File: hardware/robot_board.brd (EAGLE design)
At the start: 95.2 x 72.1 mm, 132 parts, among them J1 POWER_JACKPTH, Q1 DMP2035U, Q2 DMP2035U, Q3 DMP2035U-7, Q4 DMP2035U-7, U1 FT232RL-BASICSSOP, U11 LM393, U12 LM393, U16 LM393, U17 ATMEGA325PA, U5 SIA907EDJT, U6 SIA907EDJT

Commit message: begin power layout
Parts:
- removed IC3: (no value), v-reg:78XXS
- removed U$2: SIA907EDJT, jseng:SC70T
- removed U$7: TLV70233, jseng:SOT-23-5
- added U2: SIA907EDJT, jseng:SC70T
- added U3: MIC5219, SparkFun-PowerIC:SOT23-5
- added U7: TLV70233, jseng:SOT-23-5
- C1, C2: value (none) -> 22pF
- R1, R10, R11, R12, R13, R14, R15, R16, R17, R18, R19, R2, R20, R21, R22, R3, R4, R47, R48, R49, R5, R50, R6, R7, R8, R9: value 220 -> 300
- R25, R30, R32, R33: value (none) -> 10K
- R43: value (none) -> 1K
- R44: value (none) -> 100K
- Y1: value (none) -> 16MHz
- moved POWER 82.5 mm to (92.7, 13.0), turned to 270 degrees
- moved D25 76.2 mm to (2.54, 57.1)
- moved R41 73.4 mm to (3.81, 62.5), turned to 0 degrees
- moved R40 70.6 mm to (19.8, 68.1)
- moved R43 42.0 mm to (88.1, 10.9), turned to 270 degrees
- moved R44 38.6 mm to (88.4, 18.8), turned to 270 degrees
- moved R34 37.1 mm to (87.6, 23.6), turned to 0 degrees
- moved Q2 34.0 mm to (83.1, 21.6), turned to 0 degrees
- moved R53 26.8 mm to (53.3, 43.2), turned to 90 degrees
- moved U1 24.9 mm to (47.2, 6.60)
- moved U5 20.1 mm to (71.6, 33.0), turned to 90 degrees
- moved U6 19.8 mm to (68.6, 35.8)
- moved R39 18.0 mm to (19.8, 65.3), turned to 180 degrees
- moved R33 17.9 mm to (72.4, 40.1), turned to 90 degrees
- moved F1 15.6 mm to (75.2, 18.3), turned to 0 degrees
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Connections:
- net GYRO_INT renamed ACCEL_INT
- removed net MAIN_PWR: C3.+, D25.A, JP6.1, JP6.2, JP6.3, JP6.4, R23.2, R25.2, U$7.P$1, U$7.P$3, U$9.2, U16.8, U5.P$3, U6.P$3
- removed net N$40: Q1.2, Q2.2, R44.1
- new net PWR_SW: Q1.2, Q2.2, R44.1, U2.P$3
- new net RX: U1.1, U17.28
- new net TX: U1.5, U17.27
- net 3V3: now also U7.P$4; no longer U$7.P$4
- net 5V: now also C3.+, D25.A, JP6.1, JP6.2, JP6.3, JP6.4, R23.2, R25.2, U$9.2, U5.P$3, U6.P$3, U7.P$1, U7.P$3
- net GND: now also U3.2, U7.P$2; no longer IC3.GND, U$7.P$2
- net HIGH_5V_REG: now also U3.5; no longer IC3.OUT
- net N$28: now also U2.P$1, U2.P$4; no longer U$2.P$1, U$2.P$4
- net USBGATE: now also U2.P$2, U2.P$5; no longer U$2.P$2, U$2.P$5
- net USB_5V: now also U16.8, U2.P$6; no longer U$2.P$6
- net VIN: now also R35.2
- net VIN_F: now also U3.1, U3.3; no longer IC3.IN, R35.2, U$2.P$3
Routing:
- net VIN_F: track 0.00 -> 26.0 mm
- net GND: track 2.54 -> 20.8 mm
- net N$9: track 0.00 -> 15.9 mm
- net VIN: track 0.00 -> 9.68 mm
- net N$33: track 0.00 -> 7.73 mm
- net N$43: track 0.00 -> 6.00 mm
- net N$51: track 0.00 -> 5.14 mm
- net PWR_SW: track 0.00 -> 4.48 mm
- net 5V: track 0.00 -> 3.89 mm
- net USB_5V: track 0.00 -> 2.56 mm
- net D5: track 2.54 -> 0.00 mm
- net HIGH_5V_REG: track 0.00 -> 1.48 mm

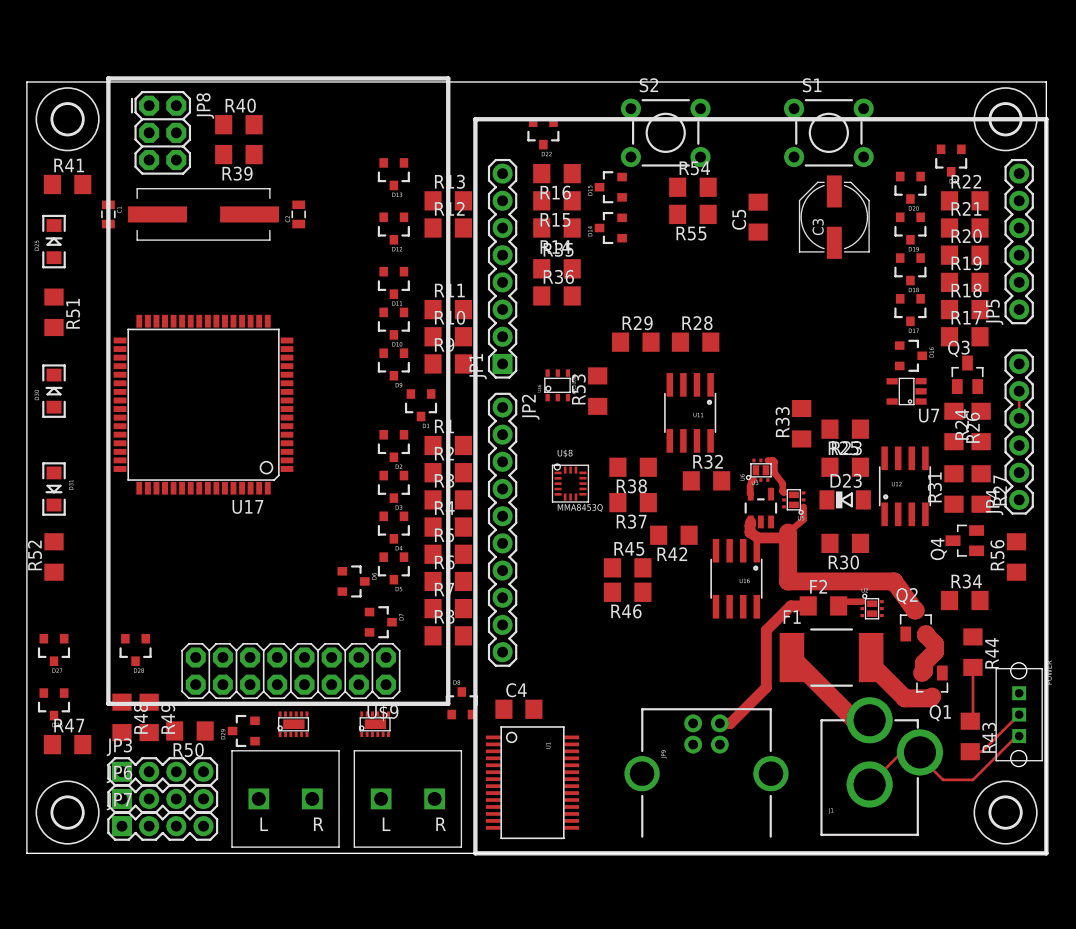
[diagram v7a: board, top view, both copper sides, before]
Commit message: more routing and library updates
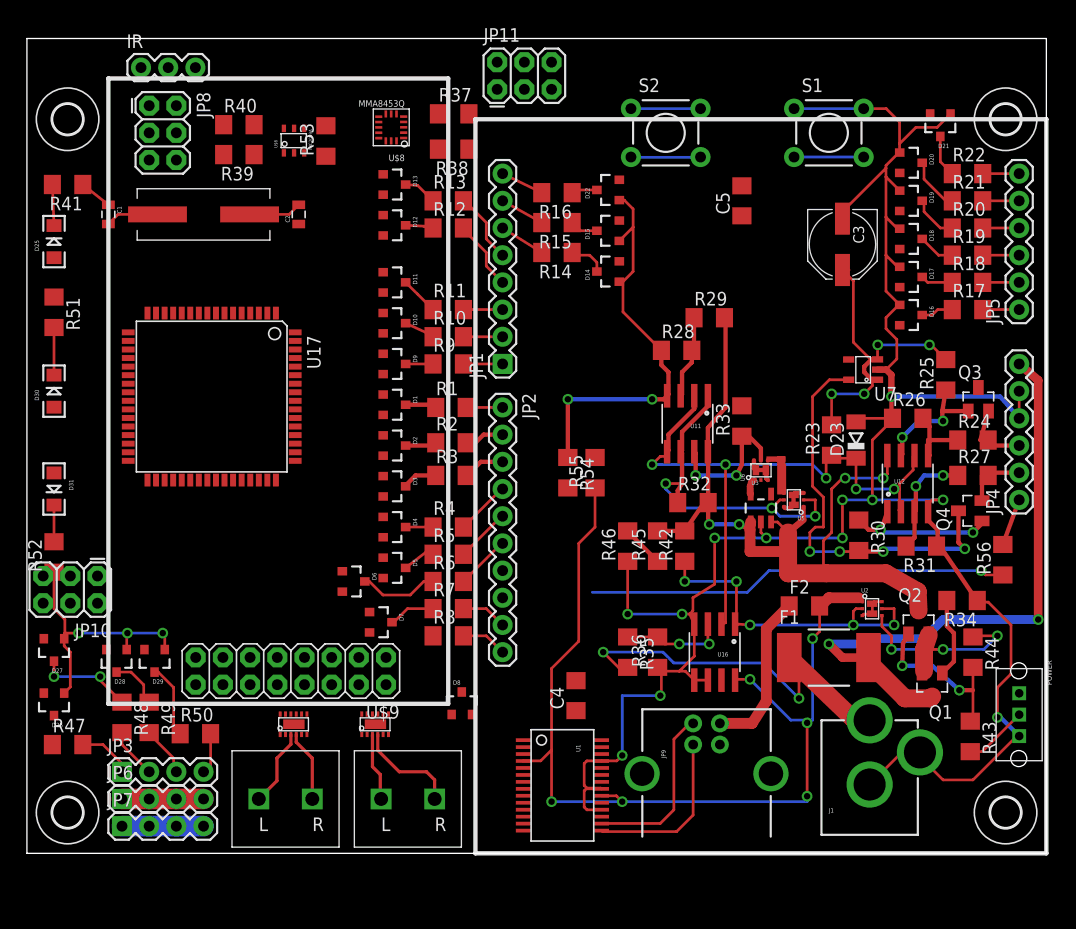
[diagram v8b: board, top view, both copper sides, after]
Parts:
- added IR: (no value), SparkFun-Connectors:1X03
- added JP10, JP11: (no value), SparkFun-Connectors:2X3
- Q3, Q4: device jseng:SOT23 -> jseng:SOT23@1
- moved R37 40.0 mm to (39.9, 69.1), turned to 0 degrees
- moved U$8 37.3 mm to (34.0, 67.8), turned to 180 degrees
- moved R35 36.4 mm to (56.1, 18.8), turned to 270 degrees
- moved R36 34.6 mm to (58.9, 18.8), turned to 90 degrees
- moved R53 34.5 mm to (27.9, 66.5)
- moved R38 34.1 mm to (39.9, 65.8)
- moved U$6 33.6 mm to (24.6, 65.8)
- moved R54 29.1 mm to (50.5, 35.6), turned to 270 degrees
- moved R55 25.8 mm to (53.1, 35.6), turned to 90 degrees
- moved R25 10.7 mm to (85.9, 44.7), turned to 90 degrees
- moved D29 10.7 mm to (11.9, 18.0), turned to 180 degrees
- moved D22 8.10 mm to (54.4, 62.0), turned to 90 degrees
- moved R29 7.23 mm to (63.8, 50.0)
- moved U16 7.15 mm to (64.3, 18.8)
- moved R31 6.14 mm to (83.6, 28.7), turned to 180 degrees
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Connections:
- net N$33: now also JP4.6
- net VIN: no longer JP4.6
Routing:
- net GND: track 20.8 -> 293.7 mm, vias 0 -> 17
- net USB_5V: track 2.56 -> 92.0 mm, vias 0 -> 6
- net 2.1V: track 0.00 -> 58.3 mm, vias 0 -> 5
- net VIN_F: track 26.0 -> 77.0 mm, vias 0 -> 4
- net N$33: track 7.73 -> 57.2 mm, vias 0 -> 2
- net RESET: track 0.00 -> 45.9 mm, vias 0 -> 1
- net 3V3: track 0.00 -> 38.4 mm, vias 0 -> 4
- net 5V: track 3.89 -> 41.5 mm, vias 0 -> 4
- net 5VREG_SWO: track 0.00 -> 32.3 mm, vias 0 -> 3
- net USBGATE: track 0.00 -> 30.5 mm, vias 0 -> 5
- net VIN: track 9.68 -> 37.1 mm, vias 0 -> 2
- net PWR_SW: track 4.48 -> 21.5 mm, vias 0 -> 3
- net N$1: track 0.00 -> 16.3 mm
- net N$2: track 0.00 -> 15.8 mm
- net N$45: track 0.00 -> 14.9 mm, vias 0 -> 2
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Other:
- board size 95.2 x 72.1 mm -> 95.2 x 76.1 mm
